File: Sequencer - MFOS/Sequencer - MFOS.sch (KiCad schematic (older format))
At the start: 70 parts, among them SW1 Forward, SW2 Back, SW4 Stop/Run, U1 40106, U2 40106, U3 4013, U4 40193

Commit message: finished sequencer schematic
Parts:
- added J22: RIN, symbol Connector:Conn_01x01_Female
- added J63: CK_RT1W, symbol Connector:Conn_01x01_Female
- added J64: CK_RT3, symbol Connector:Conn_01x01_Female
- added J65: STRN, symbol Connector:Conn_01x01_Female
- added J66: REV, symbol Connector:Conn_01x01_Female
- added J67: STP, symbol Connector:Conn_01x01_Female
- added J68: RESET, symbol Connector:Conn_01x01_Female
- added J69: RAND, symbol Connector:Conn_01x01_Female
- added unit 7 of U1
- added unit 7 of U2
- U1, U2: symbol 4xxx_IEEE:40106 -> 4xxx:40106
- gave numbers to parts that had none: 9
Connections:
- net +12V: now also U1.14 (VDD), U2.14 (VDD); no longer U1.14 (Vdd), U2.14 (Vdd)
- net CLK: now also J64.1 (Pin_1)
- net Earth: now also C7.2, SW3.1, U1.7 (VSS), U2.7 (VSS); no longer C6.2, C7.1, R15.1, R17.2, U1.7 (Vss), U2.7 (Vss)
- net REV: now also J66.1 (Pin_1)
- net RND: now also J69.1 (Pin_1)
- net STP: now also J67.1 (Pin_1)
- net at R20.1, SW4.1: now also J65.1 (Pin_1)
- net at R18.1, RV1.1, RV1.2: now also J63.1 (Pin_1)
- net at R17.1, SW3.2: now also J68.1 (Pin_1)
- net RIN: no longer names the net of D10.2 (A), R24.1
- net RIN: now also J22.1 (Pin_1)
- new net: C6.2, C7.1, R15.1, R17.2

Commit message: checked over sequencer schematic
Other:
- moved on the sheet: R9
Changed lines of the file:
@@
 L Device:R_US R9
 U 1 1 60460485
-P 1450 2650
-F 0 "R9" V 1245 2650 50  0000 C CNN
-F 1 "100K" V 1336 2650 50  0000 C CNN
-F 2 "" V 1490 2640 50  0001 C CNN
-F 3 "~" H 1450 2650 50  0001 C CNN
-	1    1450 2650
-	0    1    1    0
+P 1250 3150
+F 0 "R9" H 1100 3100 50  0000 C CNN
+F 1 "100K" H 1100 3200 50  0000 C CNN
+F 2 "" V 1290 3140 50  0001 C CNN
+F 3 "~" H 1250 3150 50  0001 C CNN
+	1    1250 3150
+	-1   0    0    1
 $EndComp
 $Comp
@@
 L power:Earth #PWR08
 U 1 1 604CA42A
-P 1650 2700
-F 0 "#PWR08" H 1650 2450 50  0001 C CNN
-F 1 "Earth" H 1650 2550 50  0001 C CNN
-F 2 "" H 1650 2700 50  0001 C CNN
-F 3 "~" H 1650 2700 50  0001 C CNN
-	1    1650 2700
-	1    0    0    -1
-$EndComp
-Wire Wire Line
-	1650 2700 1650 2650
-Wire Wire Line
-	1650 2650 1600 2650
-Wire Wire Line
-	1300 2650 1250 2650
+P 1250 3300
+F 0 "#PWR08" H 1250 3050 50  0001 C CNN
+F 1 "Earth" H 1250 3150 50  0001 C CNN
+F 2 "" H 1250 3300 50  0001 C CNN
+F 3 "~" H 1250 3300 50  0001 C CNN
+	1    1250 3300
+	1    0    0    -1
+$EndComp
 Wire Wire Line
 	1200 3000 1250 3000
 Wire Wire Line
 	1250 3000 1250 2650
-Connection ~ 1250 2650
 Wire Wire Line
 	1250 2650 1200 2650

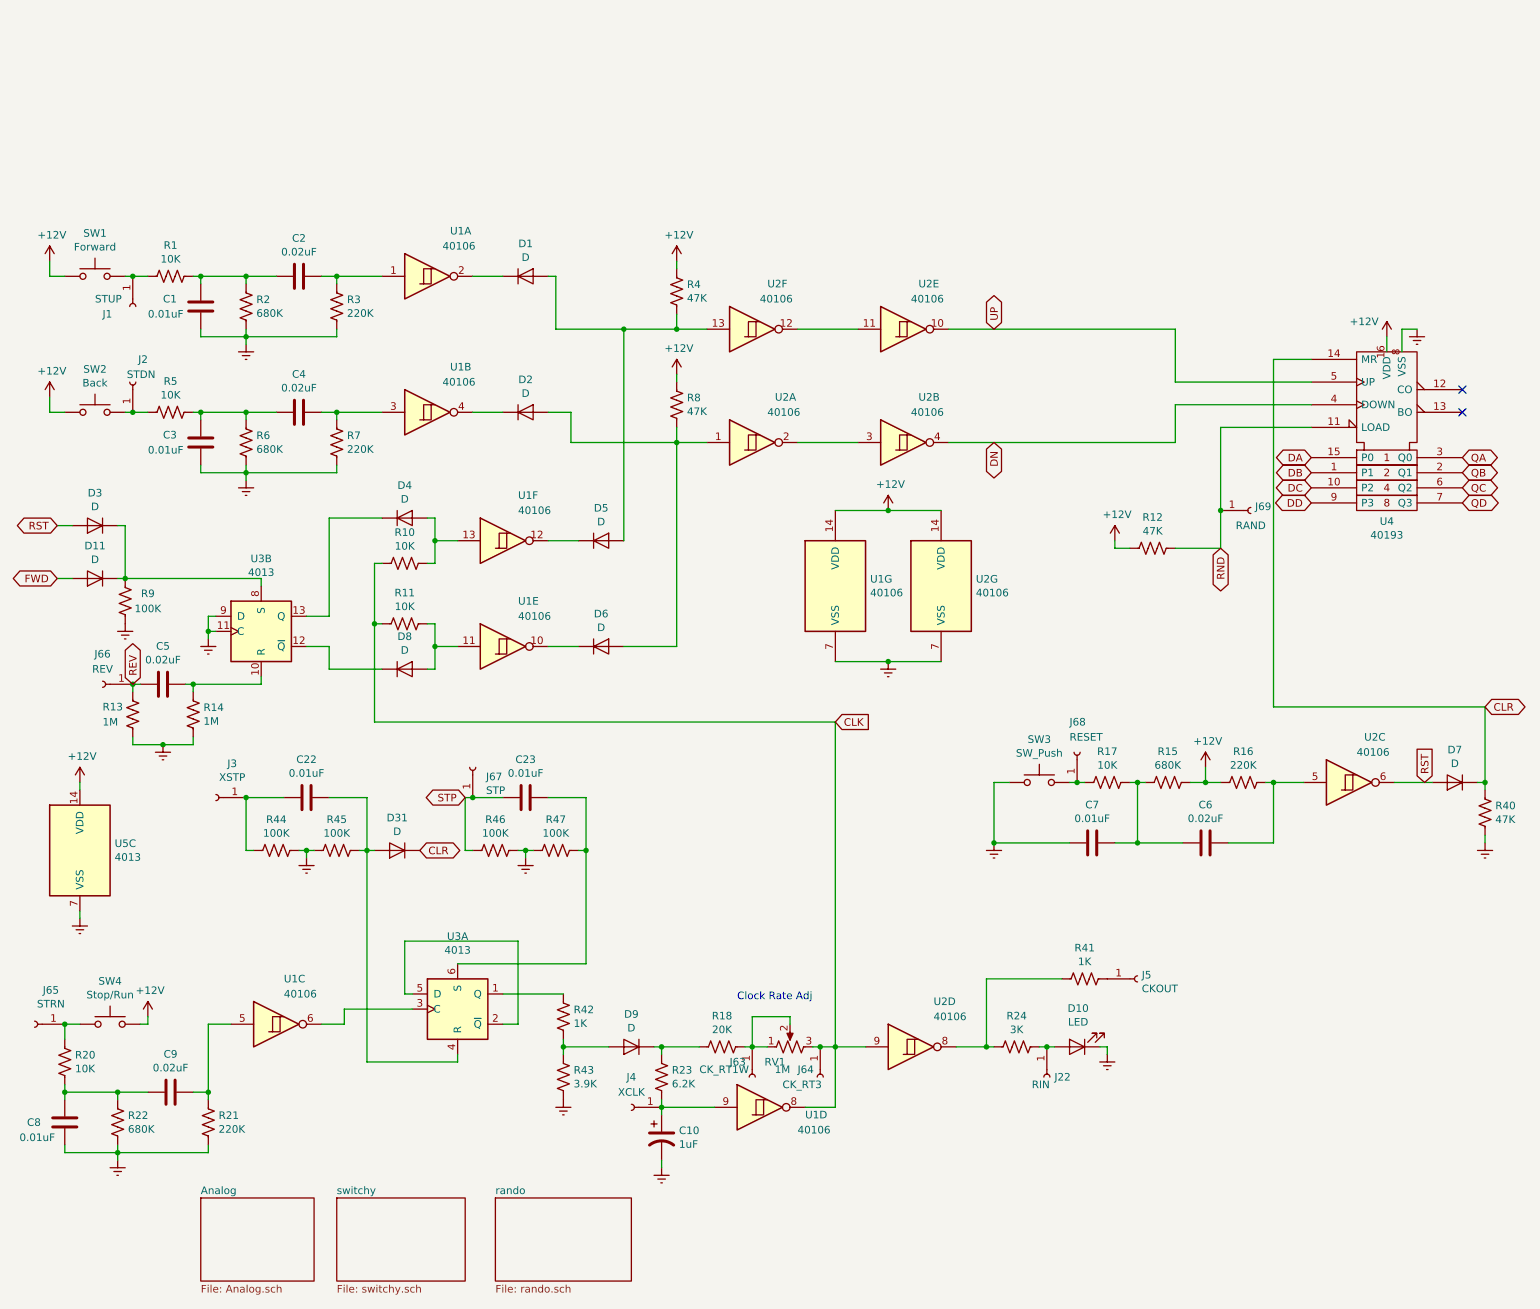
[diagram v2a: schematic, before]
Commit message: sequencer pcb designed and base silkscreen
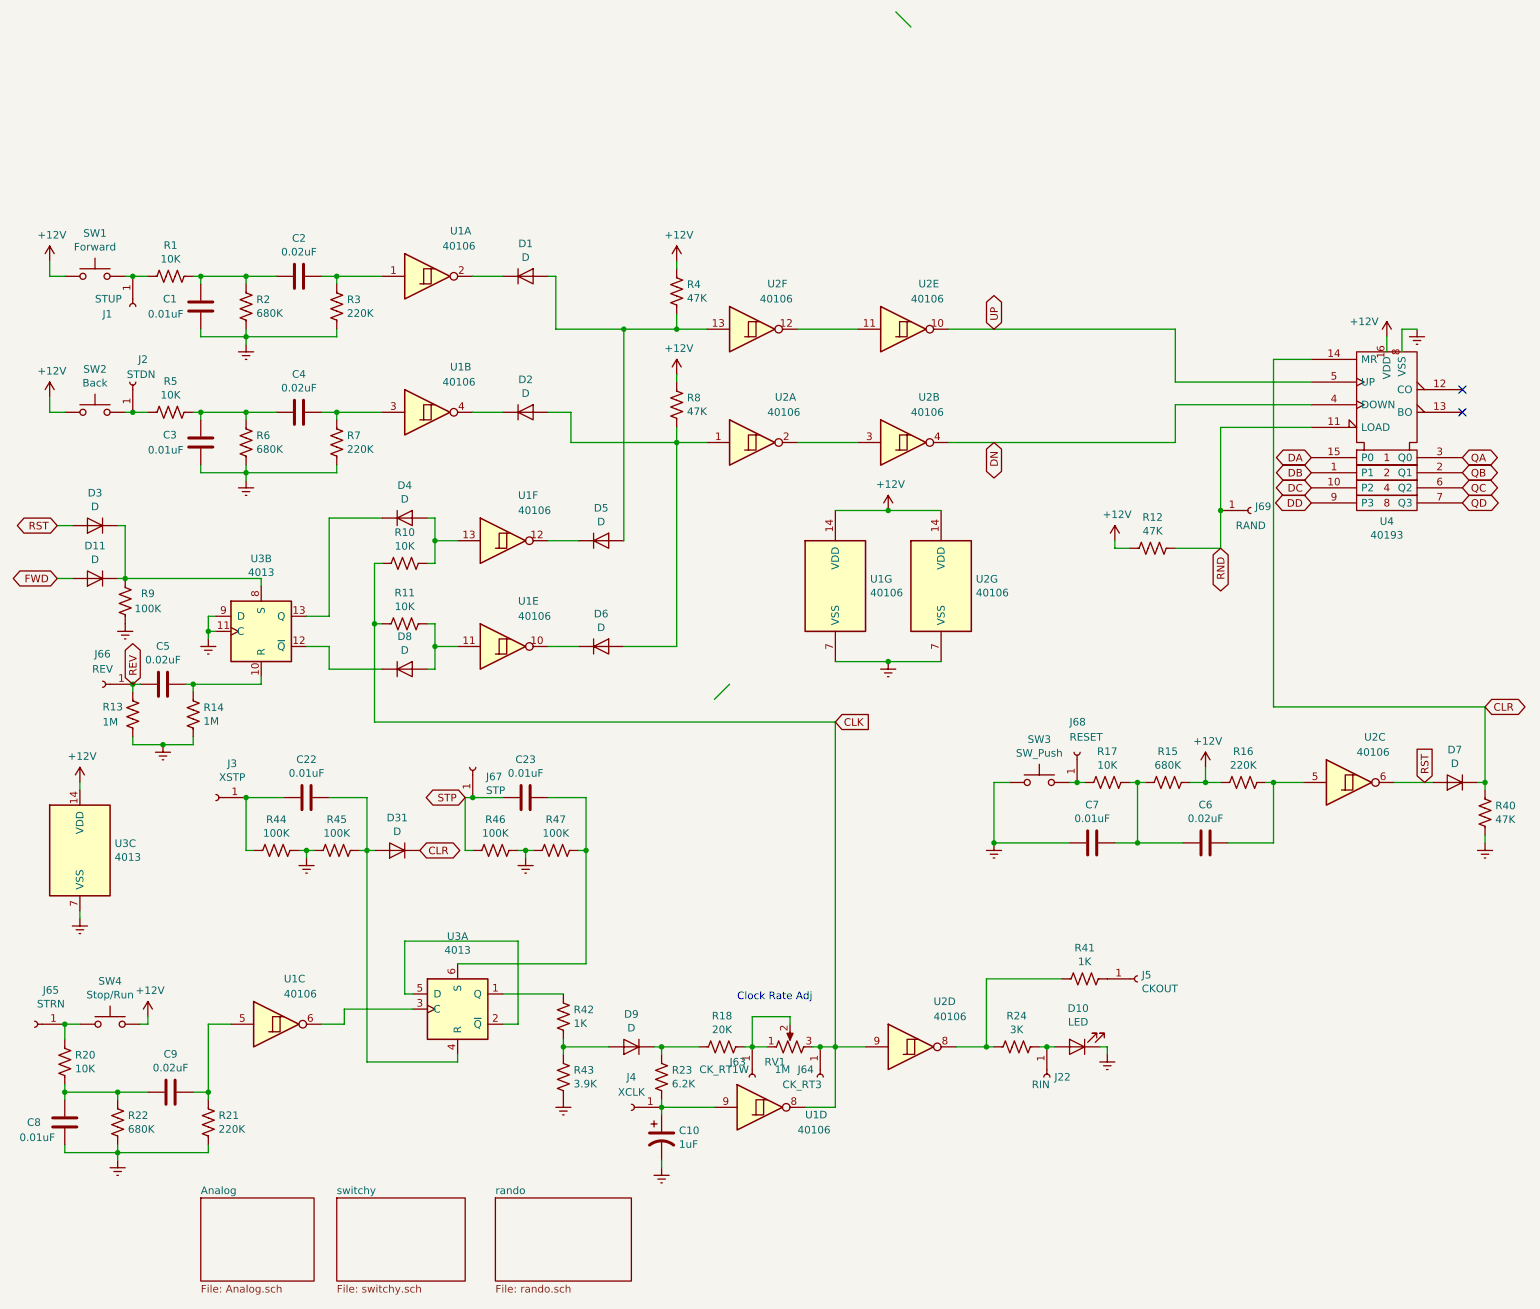
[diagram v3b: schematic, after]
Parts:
- C1, C10, C2, C22, C23, C3, C4, C5, C6, C7, C8, C9: footprint (none) -> Capacitor_THT:C_Rect_L7.0mm_W2.5mm_P5.00mm
- D1, D11, D2, D3, D31, D4, D5, D6, D7, D8, D9: footprint (none) -> Diode_THT:D_T-1_P5.08mm_Horizontal
- J1, J2, J22, J3, J4, J5, J63, J64, J65, J66, J67, J68, J69: footprint (none) -> Connector_Wire:SolderWirePad_1x01_Drill1mm
- R1, R10, R11, R12, R13, R14, R15, R16, R17, R18, R2, R20, R21, R22, R23, R24, R3, R4, R40, R41, R42, R43, R44, R45, R46, R47, R5, R6, R7, R8, R9: footprint (none) -> Resistor_THT:R_Axial_DIN0207_L6.3mm_D2.5mm_P7.62mm_Horizontal
- U1, U2, U3: footprint (none) -> Package_DIP:DIP-14_W7.62mm_Socket
- U3: renamed from U5; footprint (none) -> Package_DIP:DIP-14_W7.62mm_Socket
- U4: footprint (none) -> Package_DIP:DIP-16_W7.62mm_Socket

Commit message: ooh some new pcbs yayy
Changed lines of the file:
@@
 	3550 4450 3500 4450
-Entry Wire Line
-	5150 3800 5250 3700
 Entry Wire Line
 	6350 -750 6450 -650
